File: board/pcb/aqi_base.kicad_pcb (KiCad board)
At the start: 2 copper layers, 165.1 x 101.6 mm, 70 parts, among them U1 ESP32-DEVKITC-32D, U2 LM1117-3.3, U3 2821, U5 MIC803-29D3VC3-TR

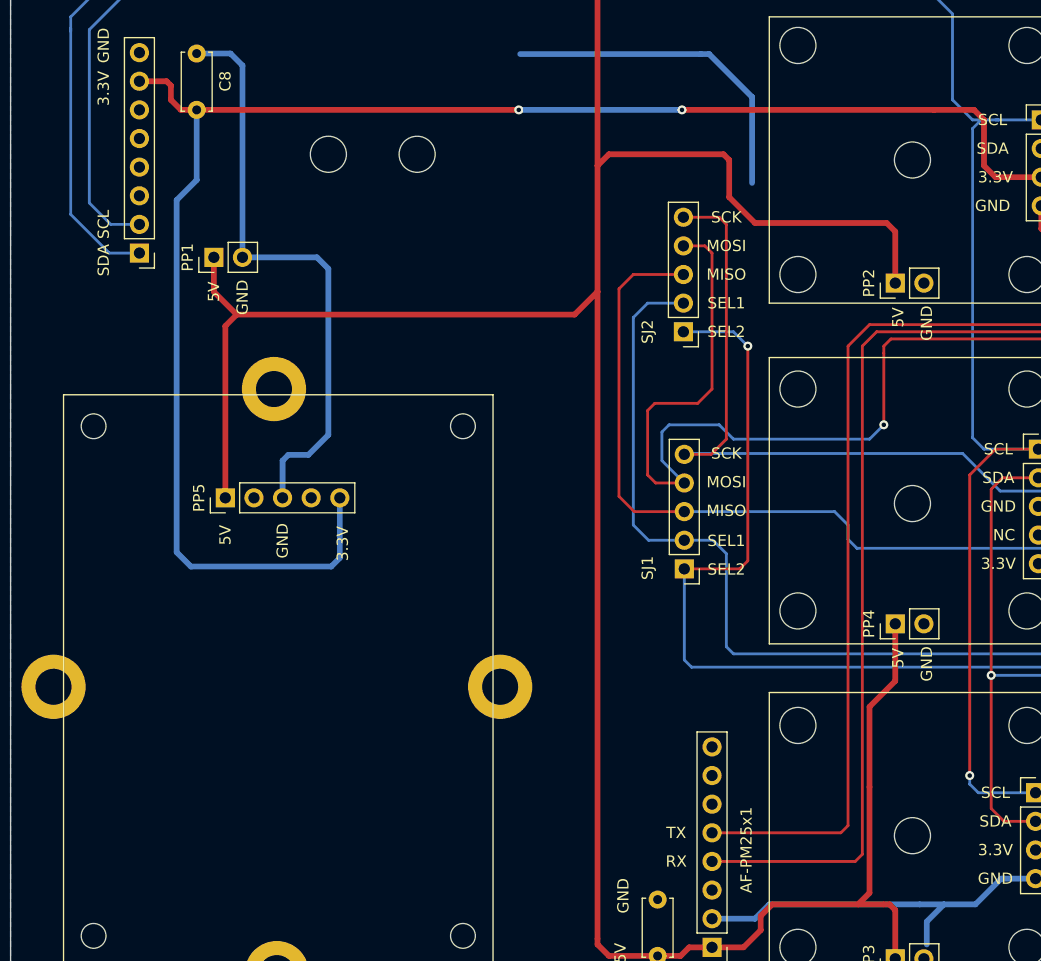
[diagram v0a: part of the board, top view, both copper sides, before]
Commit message: Update to display missing reference designators
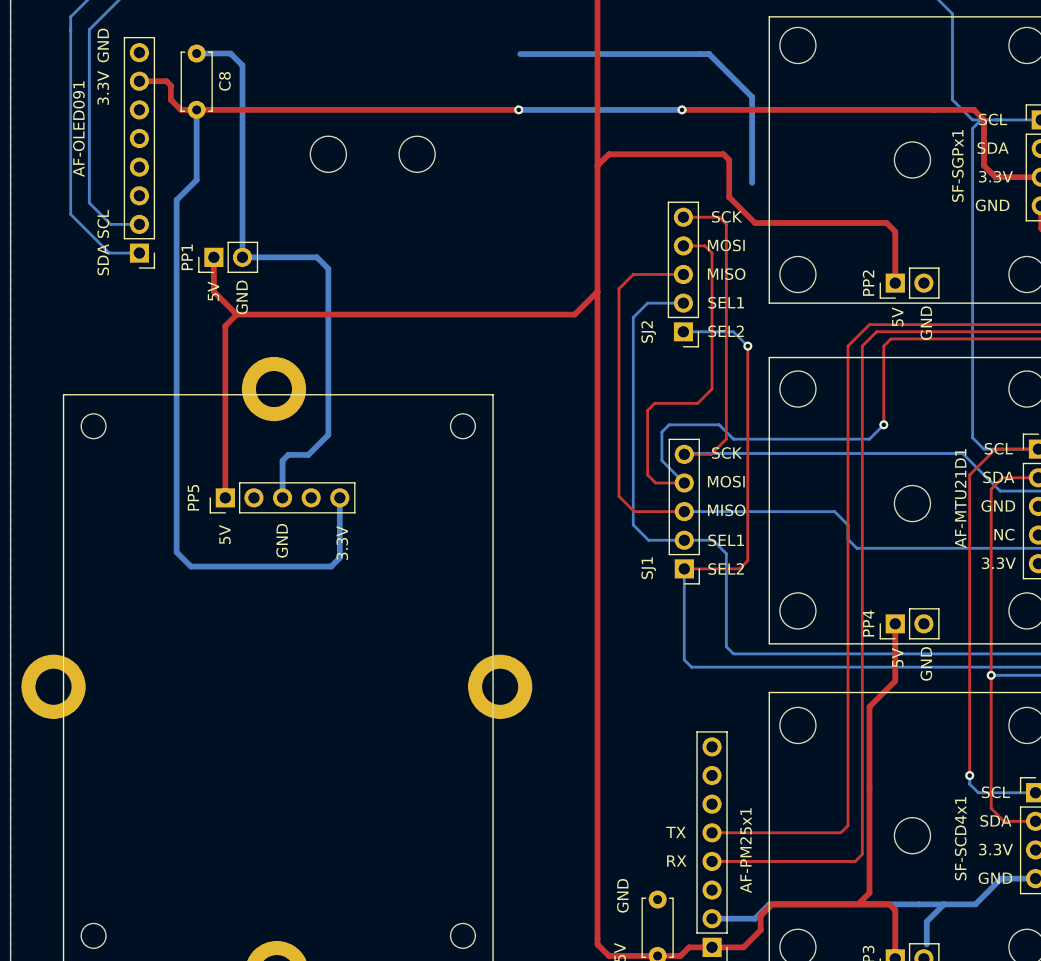
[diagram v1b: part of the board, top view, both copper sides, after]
